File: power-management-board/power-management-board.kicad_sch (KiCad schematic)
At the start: 123 parts, among them IC1 LM74502QDDFRQ1, IC2 TLP7820_TP4,E, IC3 MCP2562, J1 Conn_01x02, J2 Conn_01x02, J3 Conn_01x04, J4 Conn_01x04, J5 Conn_01x04_Pin, J6 Conn_01x02_Pin, J7 Conn_01x02, J8 Conn_01x02, J9 Conn_01x03, Q1 XPQR8308QB,LXHQ, Q2 XPQR8308QB,LXHQ, SW1 SW_Push, SW2 SW_SPDT_312, SW3 SW_SPDT_312, U1 TLP293, U2 TLP3546A, U3 STM32G431K8Tx, U4 NJM12888F33, U5 TLP293, U6 CZ3A07, U7 AP7375, U8 TLP293, U9 TLP293

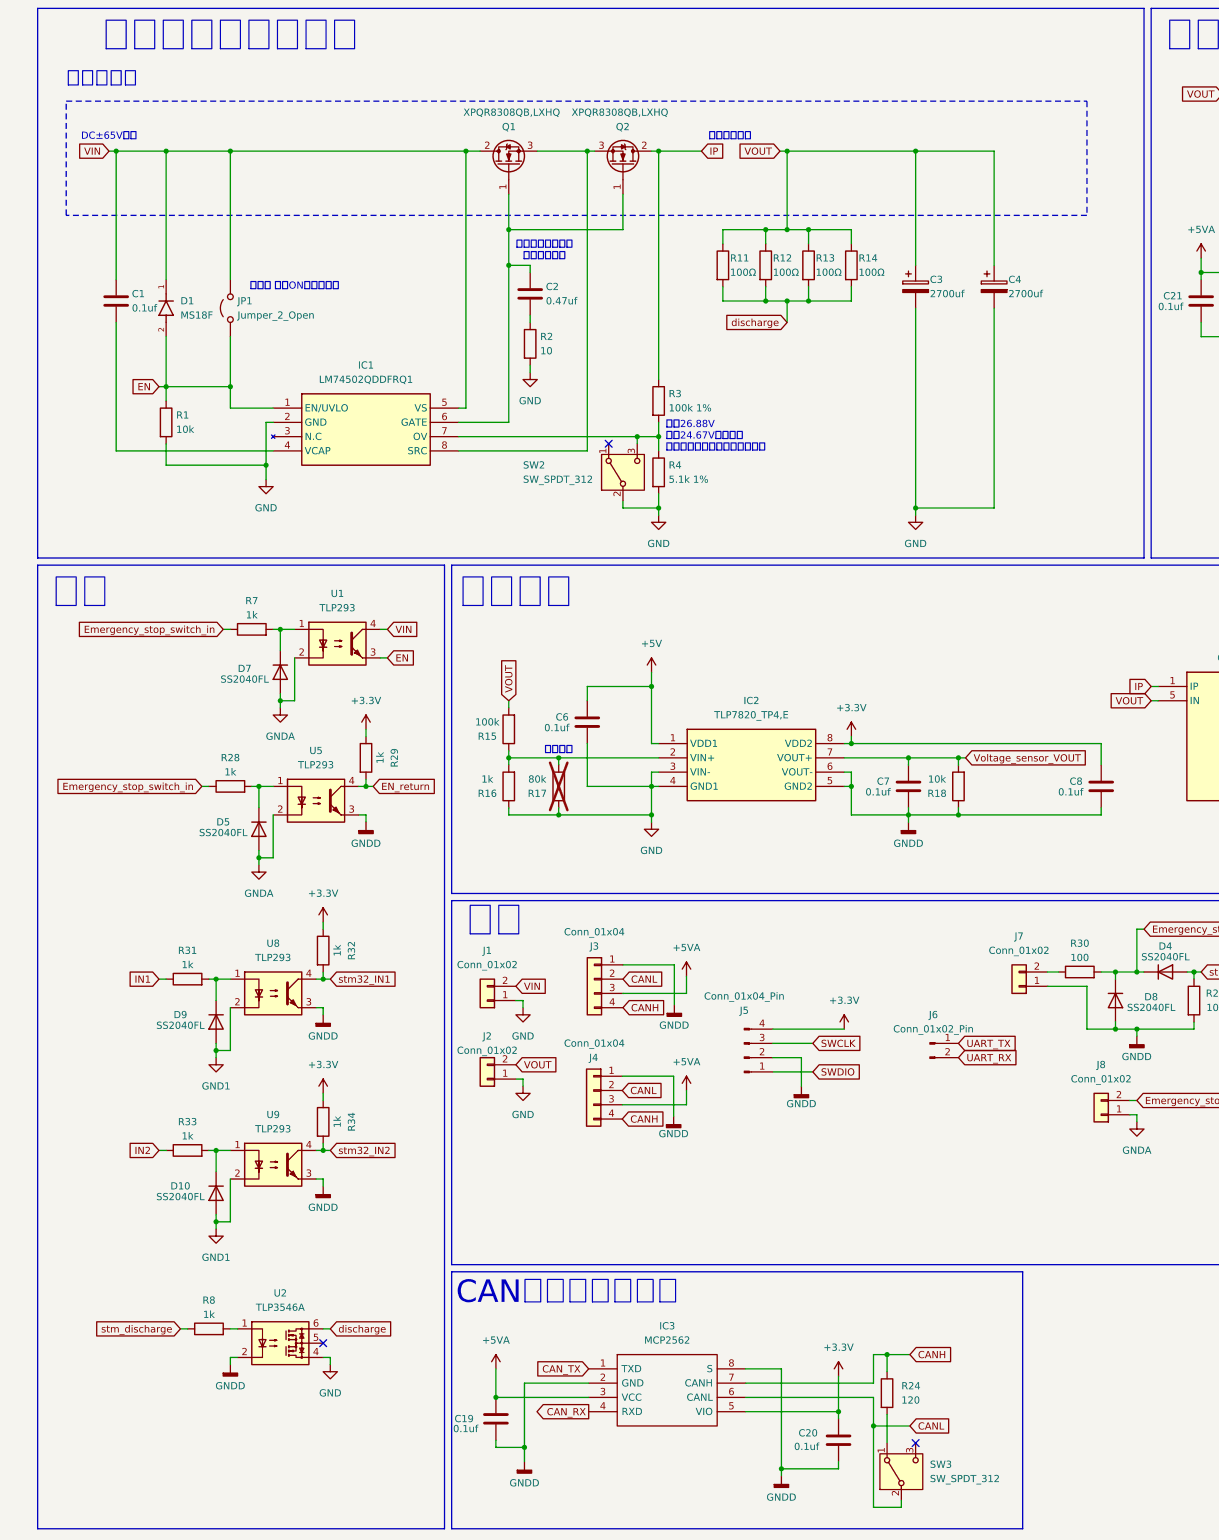
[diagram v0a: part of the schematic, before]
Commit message: LM74502QDDFRQ1からLTC4368IMS2PBFに変更
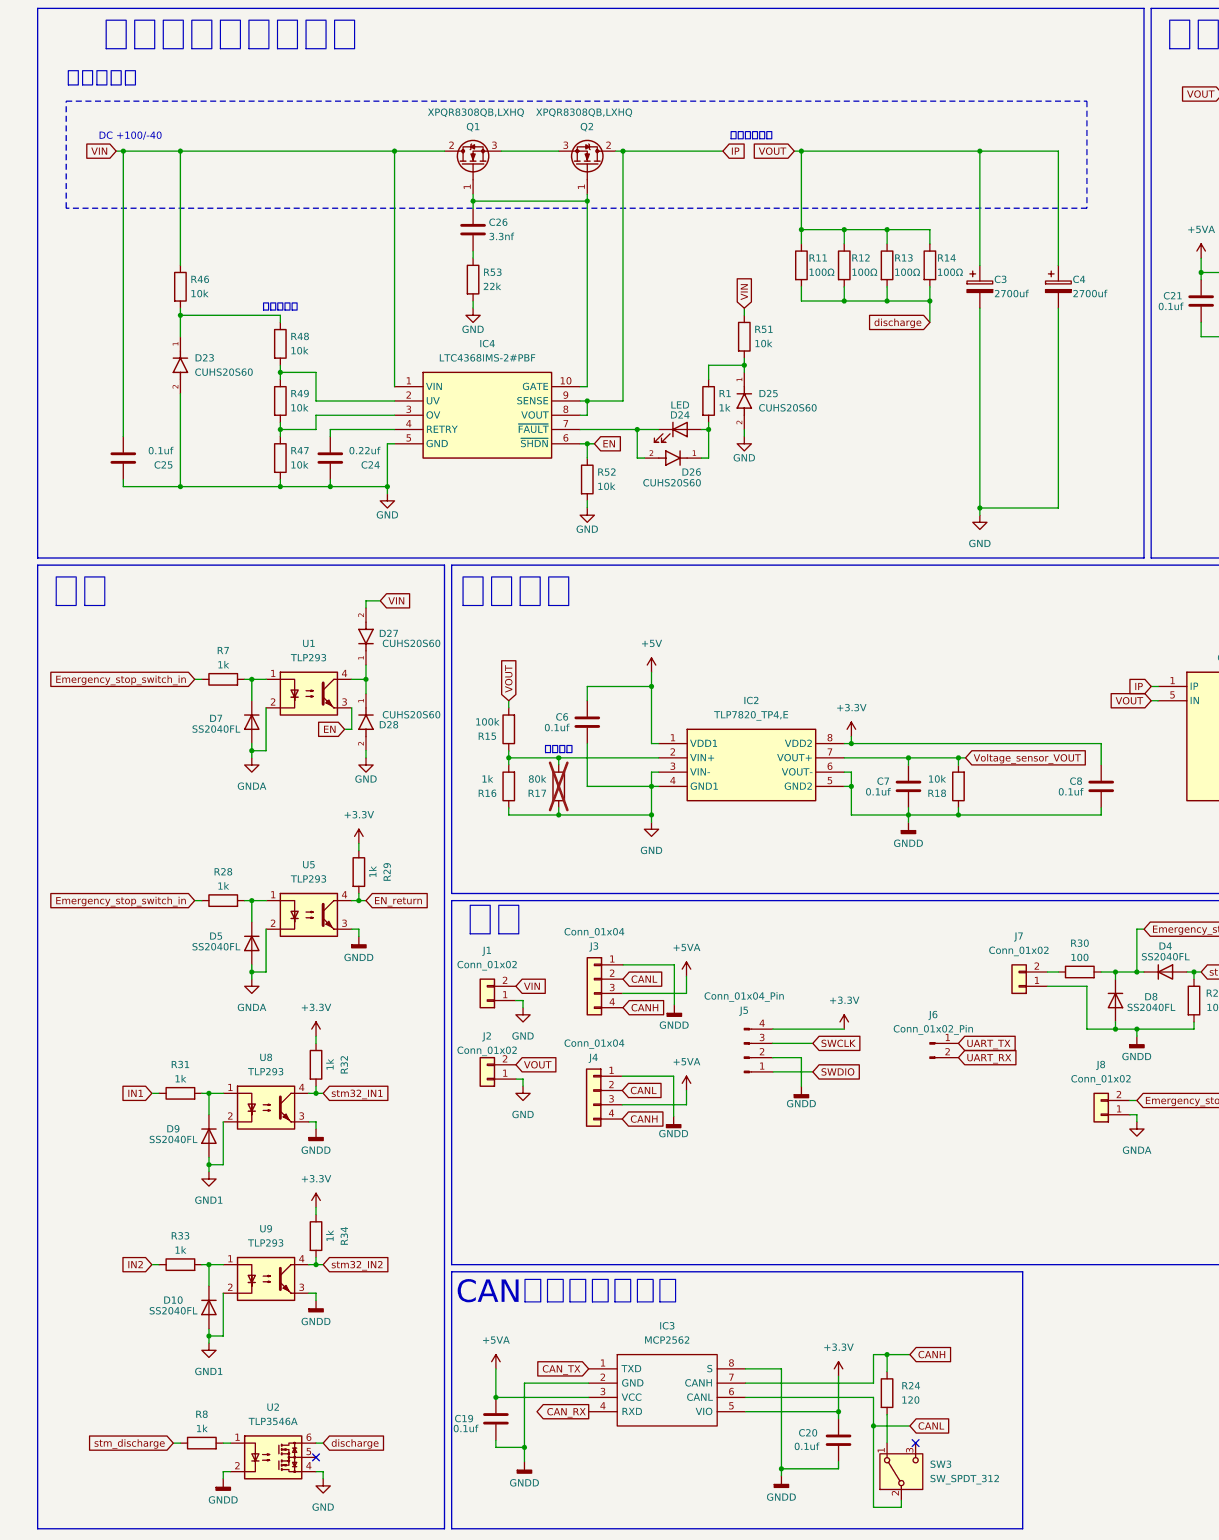
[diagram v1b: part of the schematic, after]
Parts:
- removed C1: 0.1uf, Capacitor_SMD:C_0603_1608Metric_Pad1.08x0.95mm_HandSolder, symbol Device:C
- removed C2: 0.47uf, Capacitor_SMD:C_0603_1608Metric_Pad1.08x0.95mm_HandSolder, symbol Device:C
- removed D1: MS18F, Diode_SMD:D_2010_5025Metric_Pad1.52x2.65mm_HandSolder, symbol My_Library:1N4007
- removed IC1: LM74502QDDFRQ1, Package_TO_SOT_SMD:SOT-23-8_Handsoldering, symbol LM74502QDDFRQ1:LM74502QDDFRQ1
- removed JP1: Jumper_2_Open, Connector_PinHeader_2.54mm:PinHeader_1x02_P2.54mm_Vertical, symbol Jumper:Jumper_2_Open
- removed R2: 10, Resistor_SMD:R_0603_1608Metric_Pad0.98x0.95mm_HandSolder, symbol Device:R
- removed R3: 100k 1%, Resistor_SMD:R_0603_1608Metric_Pad0.98x0.95mm_HandSolder, symbol Device:R
- removed R4: 5.1k 1%, Resistor_SMD:R_0603_1608Metric_Pad0.98x0.95mm_HandSolder, symbol Device:R
- removed SW2: SW_SPDT_312, 0Ikedalibrary:CJS1200A1, symbol Switch:SW_SPDT_312
- added C24: 0.22uf, Capacitor_SMD:C_0603_1608Metric_Pad1.08x0.95mm_HandSolder, symbol Device:C
- added C25: 0.1uf, Capacitor_SMD:C_0603_1608Metric_Pad1.08x0.95mm_HandSolder, symbol Device:C
- added C26: 3.3nf, Capacitor_SMD:C_0603_1608Metric_Pad1.08x0.95mm_HandSolder, symbol Device:C
- added D23, D25, D26, D27, D28: CUHS20S60, 0Ikedalibrary:Diode_US2H, symbol My_Library:1N4007
- added D24: LED, LED_SMD:LED_0603_1608Metric_Pad1.05x0.95mm_HandSolder, symbol Device:LED
- added IC4: LTC4368IMS-2#PBF, 0Ikedalibrary:SOP50P490X110-10N, symbol LTC4368IMS-2#PBF:LTC4368IMS-2#PBF
- added R46, R47, R48, R49, R51, R52: 10k, Resistor_SMD:R_0603_1608Metric_Pad0.98x0.95mm_HandSolder, symbol Device:R
- added R53: 22k, Resistor_SMD:R_0603_1608Metric_Pad0.98x0.95mm_HandSolder, symbol Device:R
- R1: value 10k -> 1k
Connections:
- net EN: now also IC4.6 (~{SHDN}), R52.1; no longer R1.1
- net GND: now also C24.1, C25.1, D23.2, D25.2, D28.2, IC4.5 (GND), R47.2, R52.2, R53.2; no longer R1.2
- net IP: now also IC4.8 (VOUT), IC4.9 (SENSE)
- net VIN: now also C25.2, D27.2, IC4.1 (VIN), R46.1, R51.1; no longer U1.4
- net at Q1.1 (G), Q2.1 (G): now also C26.1, IC4.10 (GATE)
- new net: D25.1, R1.1, R51.2
- new net: D24.2 (A), D26.1, R1.2
- new net: IC4.2 (UV), R48.2, R49.1
- new net: IC4.3 (OV), R47.1, R49.2
- new net: D24.1 (K), D26.2, IC4.7 (~{FAULT})
- new net: D23.1, R46.2, R48.1
- new net: C24.2, IC4.4 (RETRY)
- new net: D27.1, D28.1, U1.4
- new net: C26.2, R53.1
- no-connect marks 9 -> 8
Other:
- note added: "DC +100/-40"
- note added: "抵抗未計算"
- note removed: "DC±65V耐圧"
- note removed: "ソフトスタート用 コンデンサー"
- note removed: "最大26.88V 最小24.67V で停止 公差を守るようにお願いします"
- note removed: "非常用 常時ONジャンパー"
- moved on the sheet: C3, C4, D10, D5, D7, D9, Q1, Q2, R11, R12, R13, R14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

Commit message: 抵抗の計算完了、常時ONのジャンパーPINの追加
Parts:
- added JP1: jp, Connector_PinHeader_2.54mm:PinHeader_1x02_P2.54mm_Vertical, symbol Jumper:Jumper_2_Bridged
- C26: value 3.3nf -> 0.1uf
- R46, R49: value 10k -> 2k
- R47: value 10k -> 3k
- R48: value 10k -> 143k
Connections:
- net EN: now also JP1.2 (B)
- net at D27.1, D28.1, U1.4: now also JP1.1 (A)
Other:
- note added: "非常用"
- note removed: "抵抗未計算"
- moved on the sheet: D27, R47, R48, R49
